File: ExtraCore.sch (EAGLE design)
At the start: 19 parts, among them Y1 RESONATORSMD

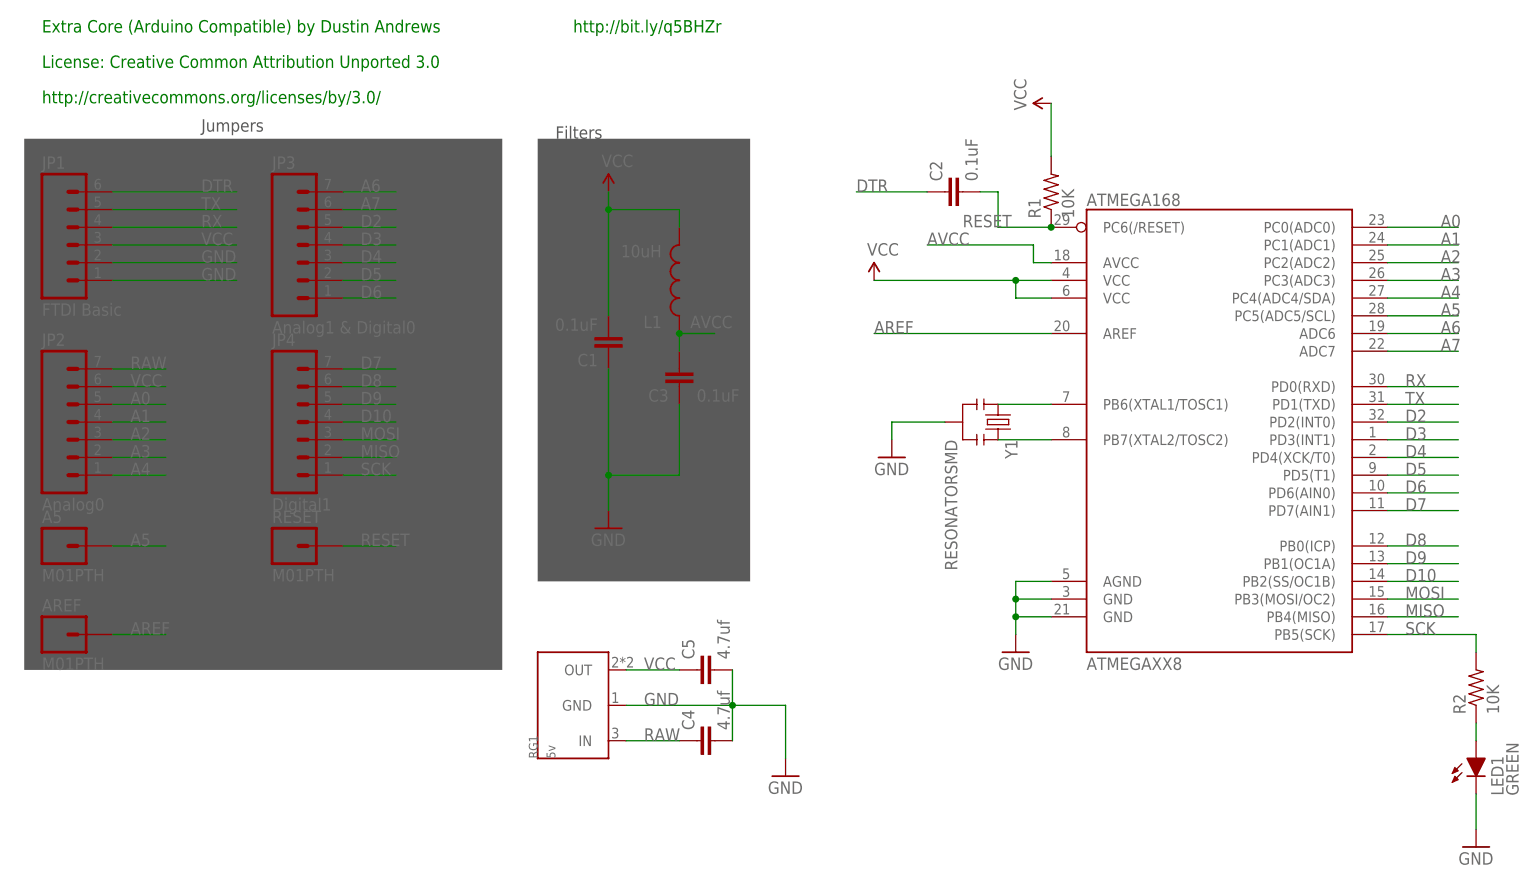
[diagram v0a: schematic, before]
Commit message: migrated to 28vqfn
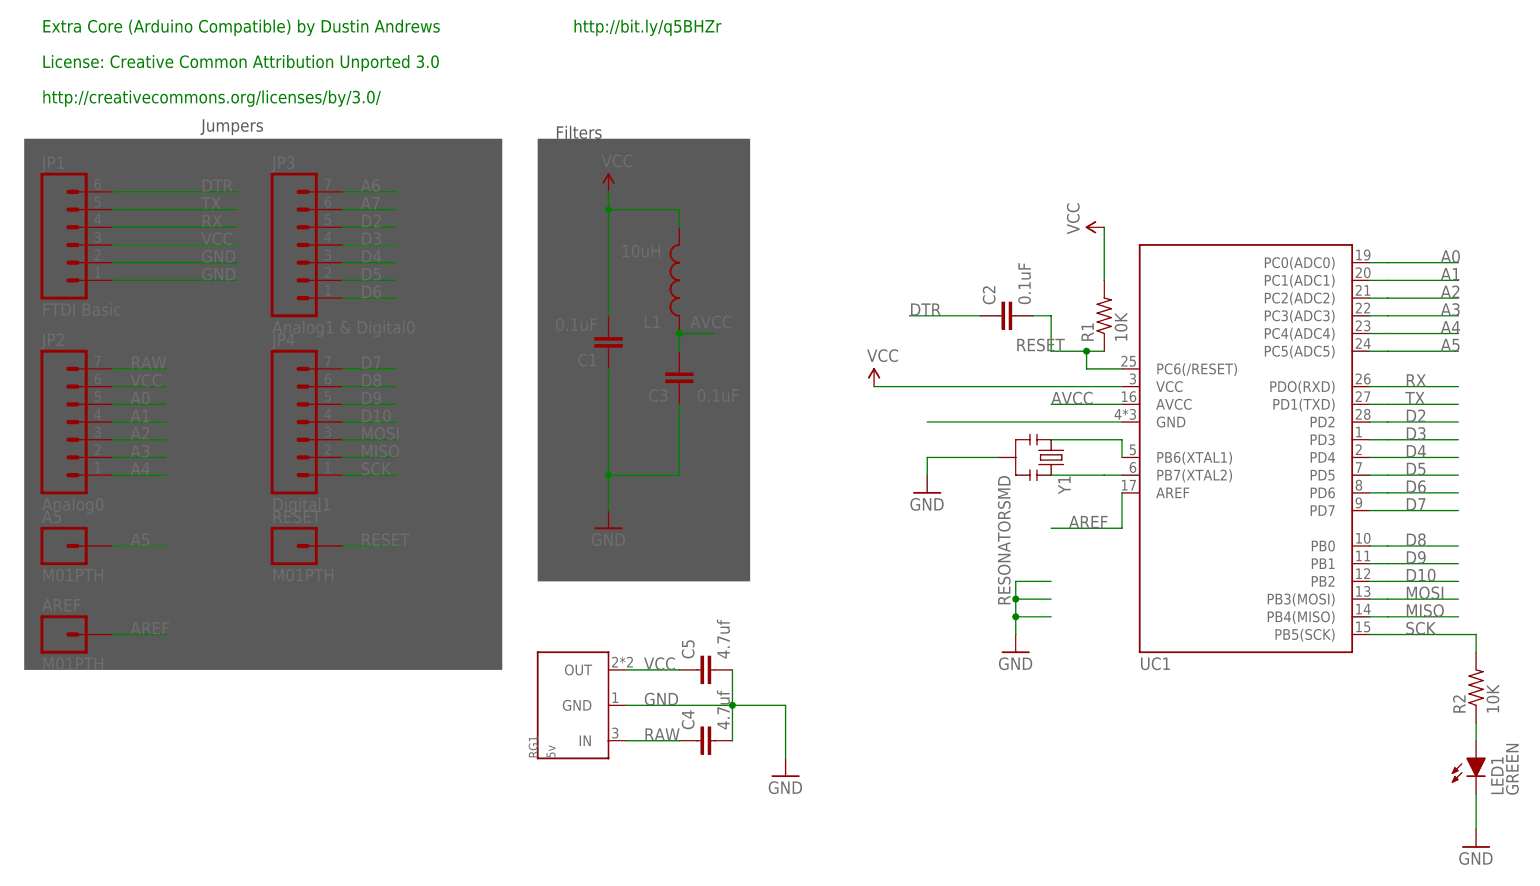
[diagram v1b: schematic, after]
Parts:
- removed ATMEGAXX8: ATMEGA168, SparkFun:ATMEGA168
- added UC1: ATMEGAXX8, Dustin:ATMEGAXX8
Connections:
- new net N$7: UC1.GND
- net A0: now also UC1.PC0(ADC0); no longer ATMEGAXX8.PC0(ADC0)
- net A1: now also UC1.PC1(ADC1); no longer ATMEGAXX8.PC1(ADC1)
- net A2: now also UC1.PC2(ADC2); no longer ATMEGAXX8.PC2(ADC2)
- net A3: now also UC1.PC3(ADC3); no longer ATMEGAXX8.PC3(ADC3)
- net A4: now also UC1.PC4(ADC4); no longer ATMEGAXX8.PC4(ADC4/SDA)
- net A5: now also UC1.PC5(ADC5); no longer ATMEGAXX8.PC5(ADC5/SCL)
- net A6: no longer ATMEGAXX8.ADC6
- net A7: no longer ATMEGAXX8.ADC7
- net AREF: now also UC1.AREF; no longer ATMEGAXX8.AREF
- net AVCC: now also UC1.AVCC; no longer ATMEGAXX8.AVCC
- net D10: now also UC1.PB2; no longer ATMEGAXX8.PB2(SS/OC1B)
- net D2: now also UC1.PD2; no longer ATMEGAXX8.PD2(INT0)
- net D3: now also UC1.PD3; no longer ATMEGAXX8.PD3(INT1)
- net D4: now also UC1.PD4; no longer ATMEGAXX8.PD4(XCK/T0)
- net D5: now also UC1.PD5; no longer ATMEGAXX8.PD5(T1)
- net D6: now also UC1.PD6; no longer ATMEGAXX8.PD6(AIN0)
- net D7: now also UC1.PD7; no longer ATMEGAXX8.PD7(AIN1)
- net D8: now also UC1.PB0; no longer ATMEGAXX8.PB0(ICP)
- net D9: now also UC1.PB1; no longer ATMEGAXX8.PB1(OC1A)
- net GND: no longer ATMEGAXX8.AGND, ATMEGAXX8.GND@1, ATMEGAXX8.GND@2
- net MISO: now also UC1.PB4(MISO); no longer ATMEGAXX8.PB4(MISO)
- net MOSI: now also UC1.PB3(MOSI); no longer ATMEGAXX8.PB3(MOSI/OC2)
- net N$3: now also UC1.PB6(XTAL1); no longer ATMEGAXX8.PB6(XTAL1/TOSC1)
- net N$4: now also UC1.PB7(XTAL2); no longer ATMEGAXX8.PB7(XTAL2/TOSC2)
- net RESET: now also UC1.PC6(/RESET); no longer ATMEGAXX8.PC6(/RESET)
- net RX: now also UC1.PDO(RXD); no longer ATMEGAXX8.PD0(RXD)
- net SCK: now also UC1.PB5(SCK); no longer ATMEGAXX8.PB5(SCK)
- net TX: now also UC1.PD1(TXD); no longer ATMEGAXX8.PD1(TXD)
- net VCC: now also UC1.VCC; no longer ATMEGAXX8.VCC@1, ATMEGAXX8.VCC@2
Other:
- moved on the sheet: C2, R1, Y1

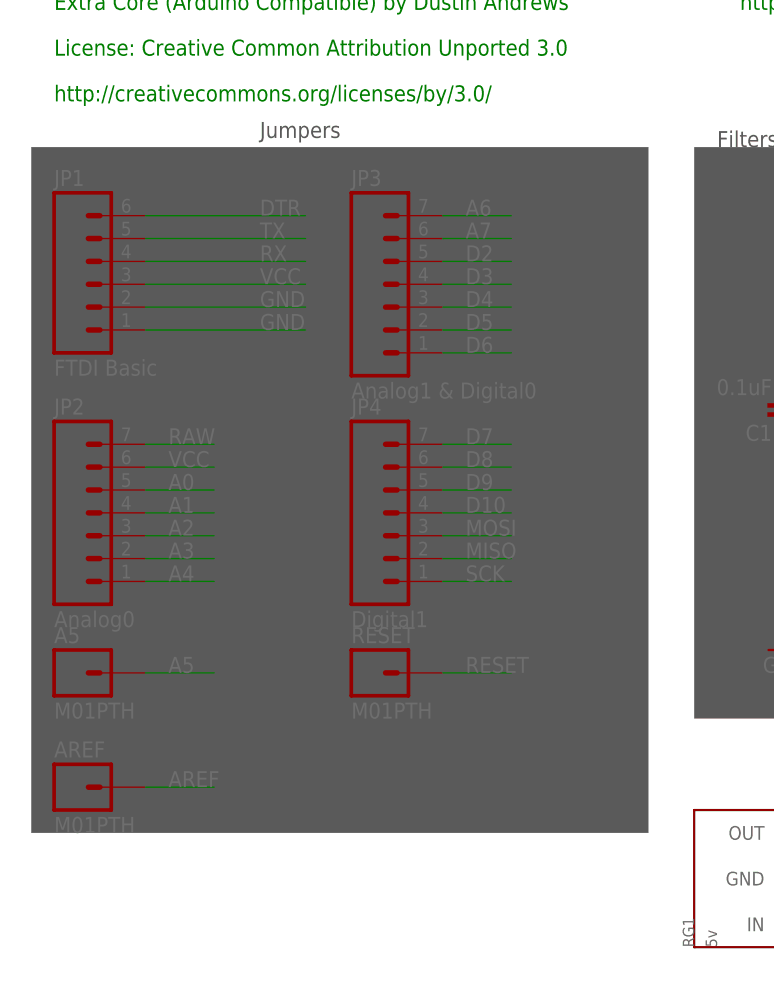
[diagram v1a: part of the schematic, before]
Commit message: changed all headers to 2mm
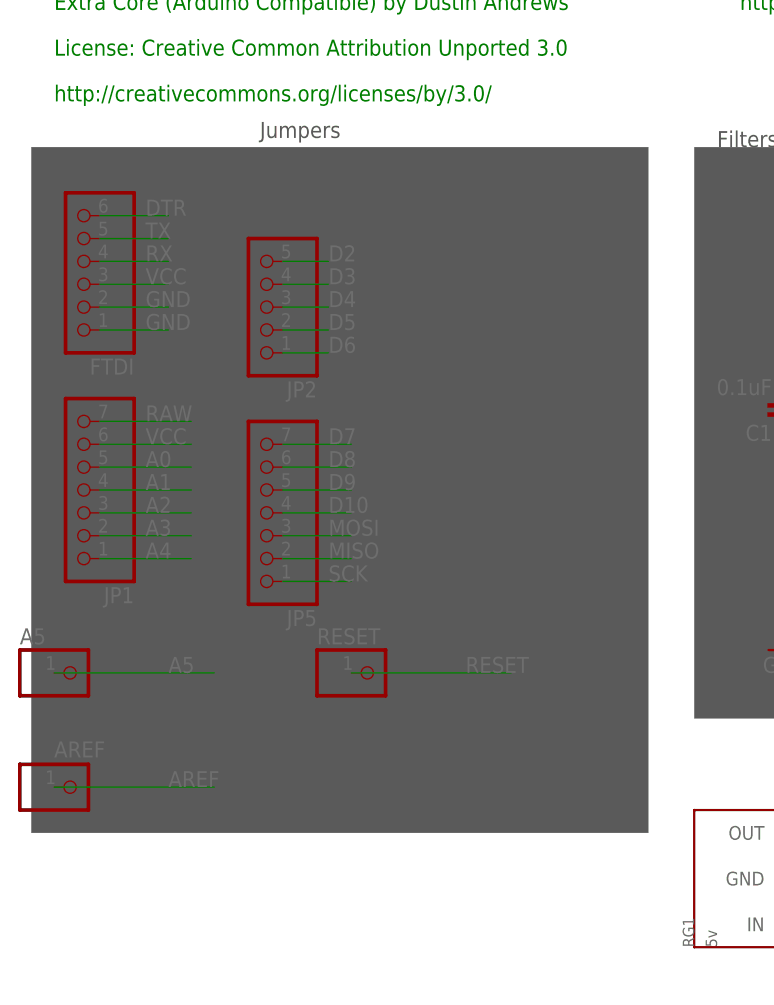
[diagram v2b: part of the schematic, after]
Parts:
- removed JP3: Analog1 & Digital0, SparkFun:M07
- removed JP4: Digital1, SparkFun:M07
- added FTDI: (no value), pinhead:PINHD-1X6M
- added JP5: (no value), pinhead:PINHD-1X7M
- A5, AREF, RESET: value M01PTH -> (none); device SparkFun:M01PTH -> pinhead:PINHD-1X1M
- JP1: value FTDI Basic -> (none); device SparkFun:M06SIP -> pinhead:PINHD-1X7M
- JP2: value Analog0 -> (none); device SparkFun:M07 -> pinhead:PINHD-1X5M
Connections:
- removed net A6: JP3.7
- removed net A7: JP3.6
- net A0: now also JP1.5; no longer JP2.5
- net A1: now also JP1.4; no longer JP2.4
- net A2: now also JP1.3; no longer JP2.3
- net A3: now also JP1.2; no longer JP2.2
- net A4: now also JP1.1; no longer JP2.1
- net D10: now also JP5.4; no longer JP4.4
- net D2: now also JP2.5; no longer JP3.5
- net D3: now also JP2.4; no longer JP3.4
- net D4: now also JP2.3; no longer JP3.3
- net D5: now also JP2.2; no longer JP3.2
- net D6: now also JP2.1; no longer JP3.1
- net D7: now also JP5.7; no longer JP4.7
- net D8: now also JP5.6; no longer JP4.6
- net D9: now also JP5.5; no longer JP4.5
- net DTR: now also FTDI.6; no longer JP1.6
- net GND: now also FTDI.1, FTDI.2; no longer JP1.1, JP1.2
- net MISO: now also JP5.2; no longer JP4.2
- net MOSI: now also JP5.3; no longer JP4.3
- net RAW: now also JP1.7; no longer JP2.7
- net RX: now also FTDI.4; no longer JP1.4
- net SCK: now also JP5.1; no longer JP4.1
- net TX: now also FTDI.5; no longer JP1.5
- net VCC: now also FTDI.3, JP1.6; no longer JP1.3, JP2.6

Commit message: moved stuff around. It's close to routable I think.
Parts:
- removed LED1: GREEN, ExtraCore:LED1206
- added LED2: (no value), SparkFun-LED:LED0603
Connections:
- net GND: now also LED2.C; no longer LED1.K
- net N$6: now also LED2.A; no longer LED1.A
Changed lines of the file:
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@@
 <part name="RESET" library="pinhead" deviceset="PINHD-1X1" device="M"/>
 <part name="L1" library="SparkFun" deviceset="INDUCTOR" device="0805" value="10uH"/>
-<part name="LED1" library="ExtraCore" deviceset="LED" device="1206" value="GREEN"/>
 <part name="RG1" library="Dustin" deviceset="LDO_VREG_3PIN" device="" value="5v"/>
 <part name="C4" library="SparkFun-Passives" deviceset="CAP" device="0805" value="4.7uf"/>
@@
 <part name="JP2" library="pinhead" deviceset="PINHD-1X5" device="M"/>
 <part name="JP5" library="pinhead" deviceset="PINHD-1X7" device="M"/>
+<part name="LED2" library="SparkFun-LED" deviceset="LED" device="0603"/>
 </parts>
 <sheets>
@@
 <instance part="RESET" gate="G$1" x="-60.96" y="43.18"/>
 <instance part="L1" gate="G$1" x="-5.08" y="81.28" rot="R180"/>
-<instance part="LED1" gate="A" x="109.22" y="10.16"/>
 <instance part="RG1" gate="G$1" x="-15.24" y="20.32" rot="R90"/>
 <instance part="C4" gate="G$1" x="0" y="15.24" rot="R90"/>
@@
 <instance part="JP2" gate="A" x="-73.66" y="83.82" rot="R180"/>
 <instance part="JP5" gate="A" x="-73.66" y="60.96" rot="R180"/>
+<instance part="LED2" gate="G$1" x="109.22" y="12.7"/>
 </instances>
 <busses>
@@
 <wire x1="109.22" y1="7.62" x2="109.22" y2="2.54" width="0.1524" layer="91"/>
 <pinref part="GND3" gate="1" pin="GND"/>
-<pinref part="LED1" gate="A" pin="K"/>
+<pinref part="LED2" gate="G$1" pin="C"/>
 </segment>
 <segment>
@@
 <wire x1="109.22" y1="17.78" x2="109.22" y2="15.24" width="0.1524" layer="91"/>
 <pinref part="R2" gate="G$1" pin="1"/>
-<pinref part="LED1" gate="A" pin="A"/>
-</segment>
-</net>
+<pinref part="LED2" gate="G$1" pin="A"/>
+</segment>
+</net>
